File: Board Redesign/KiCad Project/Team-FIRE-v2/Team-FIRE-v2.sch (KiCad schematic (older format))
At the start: 0 parts

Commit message: Added 9523 User Manual
- Added 9523 User manual
- Started work on redesign schematic
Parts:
- added C?: 10uF, Capacitor_SMD:C_0603_1608Metric, symbol Device:C
- added C?: 0.1uF, Capacitor_SMD:C_0603_1608Metric, symbol Device:C
- added C?: 22nF, Capacitor_SMD:C_0603_1608Metric, symbol Device:C
- added C?: 50pF, Capacitor_SMD:C_0603_1608Metric, symbol Device:C
- added C?: 1uF, Capacitor_SMD:C_0603_1608Metric, symbol Device:C
- added C?: 0.1u, Capacitor_SMD:C_0603_1608Metric, symbol Device:C
- added IC?: LT3959EUHE#PBF, Team-FIRE:LT3959EUHEPBF, symbol Team-FIRE:LT3959EUHE#PBF
- added J?: SIM_Card, symbol Connector:SIM_Card
- added R?: 10k, Resistor_SMD:R_0603_1608Metric, symbol Device:R
- added R? (x2): 3.3k, Resistor_SMD:R_0603_1608Metric, symbol Device:R
- added R?: 59k, Resistor_SMD:R_0603_1608Metric, symbol Device:R
- added U?: NCN4555MN, Package_DFN_QFN:QFN-16-1EP_3x3mm_P0.5mm_EP1.75x1.75mm, symbol Logic_LevelTranslator:NCN4555MN
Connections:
- new net: IC?.28 (DRIVE), R?.1
- new net: C?.2, IC?.30 (VC), R?.2
- new net: C?.1, IC?.32 (SS)
- new net: IC?.33 (RT), R?.2
- new net: C?.1, IC?.36 (INTVCC), R?.1
- new net: C?.2, R?.1
- new net +30V: IC?.31 (FBX), R?.1, R?.2
- new net GND: C?.2, C?.2, IC?.13 (GND_1), IC?.14 (GND_2), IC?.15 (GND_3), IC?.16 (GND_4), IC?.17 (GND_5), J?.5 (GND), U?.10 (GND), U?.17 (GND)
- new net GNDA: C?.1, C?.1, C?.2, C?.2, R?.2
- new net GNDS: IC?.1 (NC_1), IC?.12 (GNDK), IC?.2 (NC_2), IC?.23 (NC_6), IC?.24 (SGND_2), IC?.3 (NC_3), IC?.34 (SYNC), IC?.37 (SGND_3), IC?.4 (SGND_1), IC?.6 (NC_4)
- new net IR_5V: C?.1, U?.3 (VDD), U?.5 (VBAT)
- new net IR_SIM_CLK: U?.13 (CLK)
- new net IR_SIM_IO: U?.15 (I/O)
- new net IR_SIM_RESET: U?.14 (RST)
- new net IR_SIM_VCC: U?.2 (MOD_VCC)
- new net SIM_CLOCK: J?.3 (CLK), U?.11 (SIM_CLK)
- new net SIM_IO: J?.7 (I/O), U?.8 (SIM_I/O)
- new net SIM_RESET: J?.2 (RST), U?.9 (SIM_RST)
- new net SIM_VCC: C?.1, J?.1 (VCC), U?.7 (SIM_VCC)
- no-connect marks 0 -> 1
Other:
- note added: "LT3959 Boost"
- note added: "SIM NCN4555 & Card Holder\n"

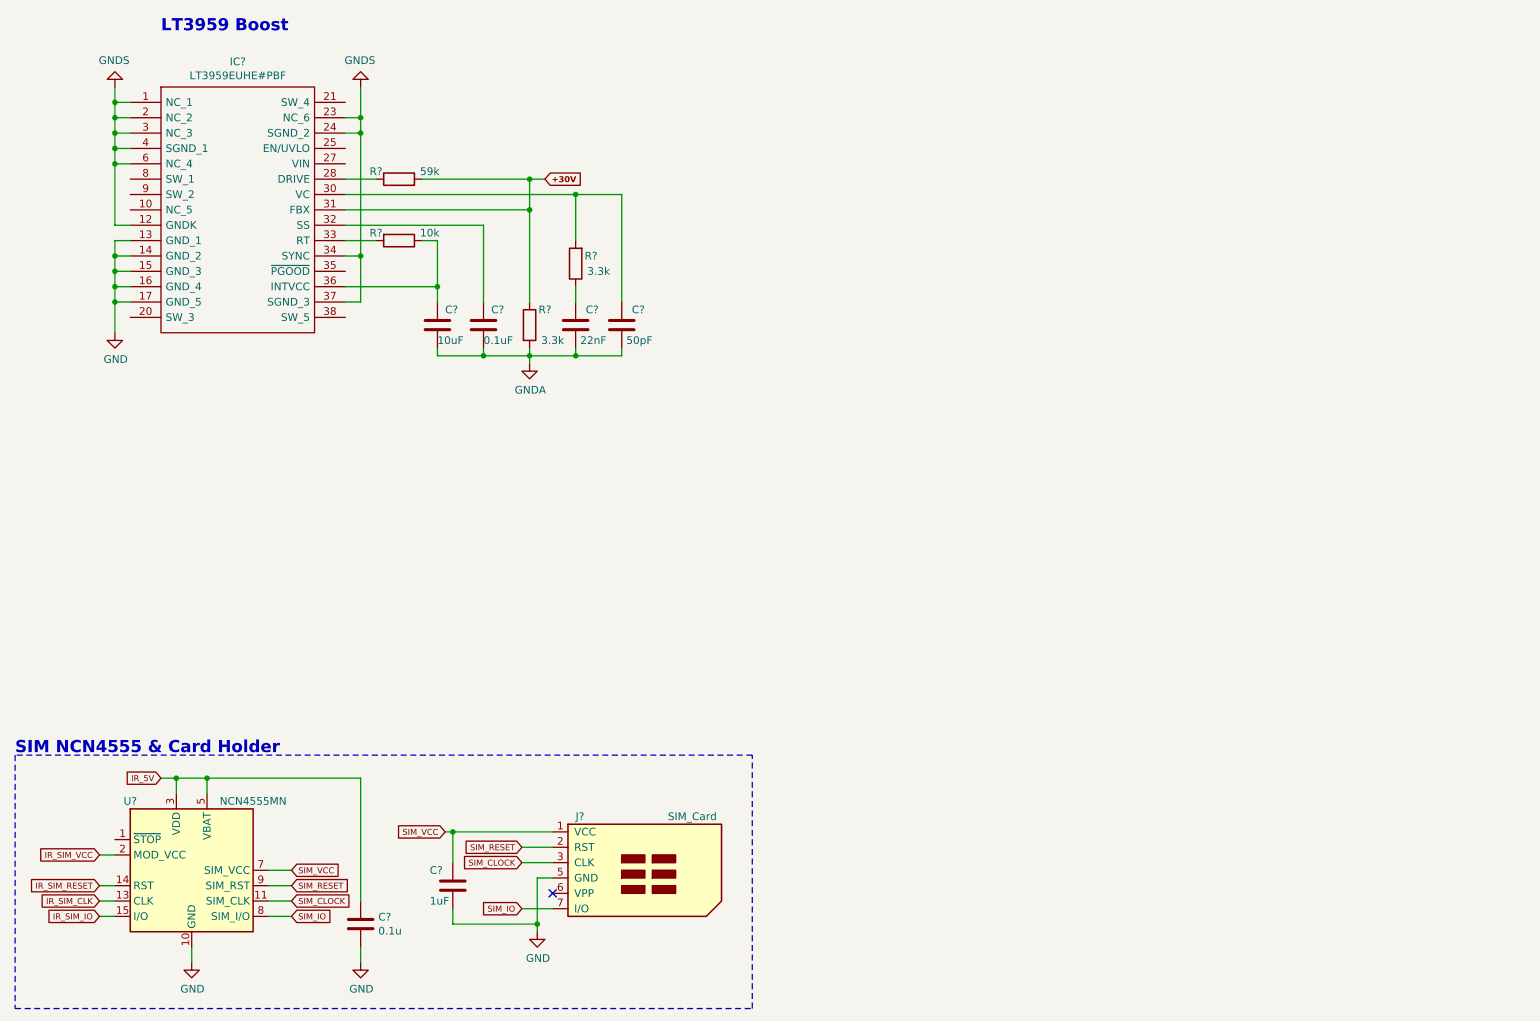
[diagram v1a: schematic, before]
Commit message: Worked more on board!
- Moved more of the schematic over to KiCad
- Created models and footprints / symbols for a few components
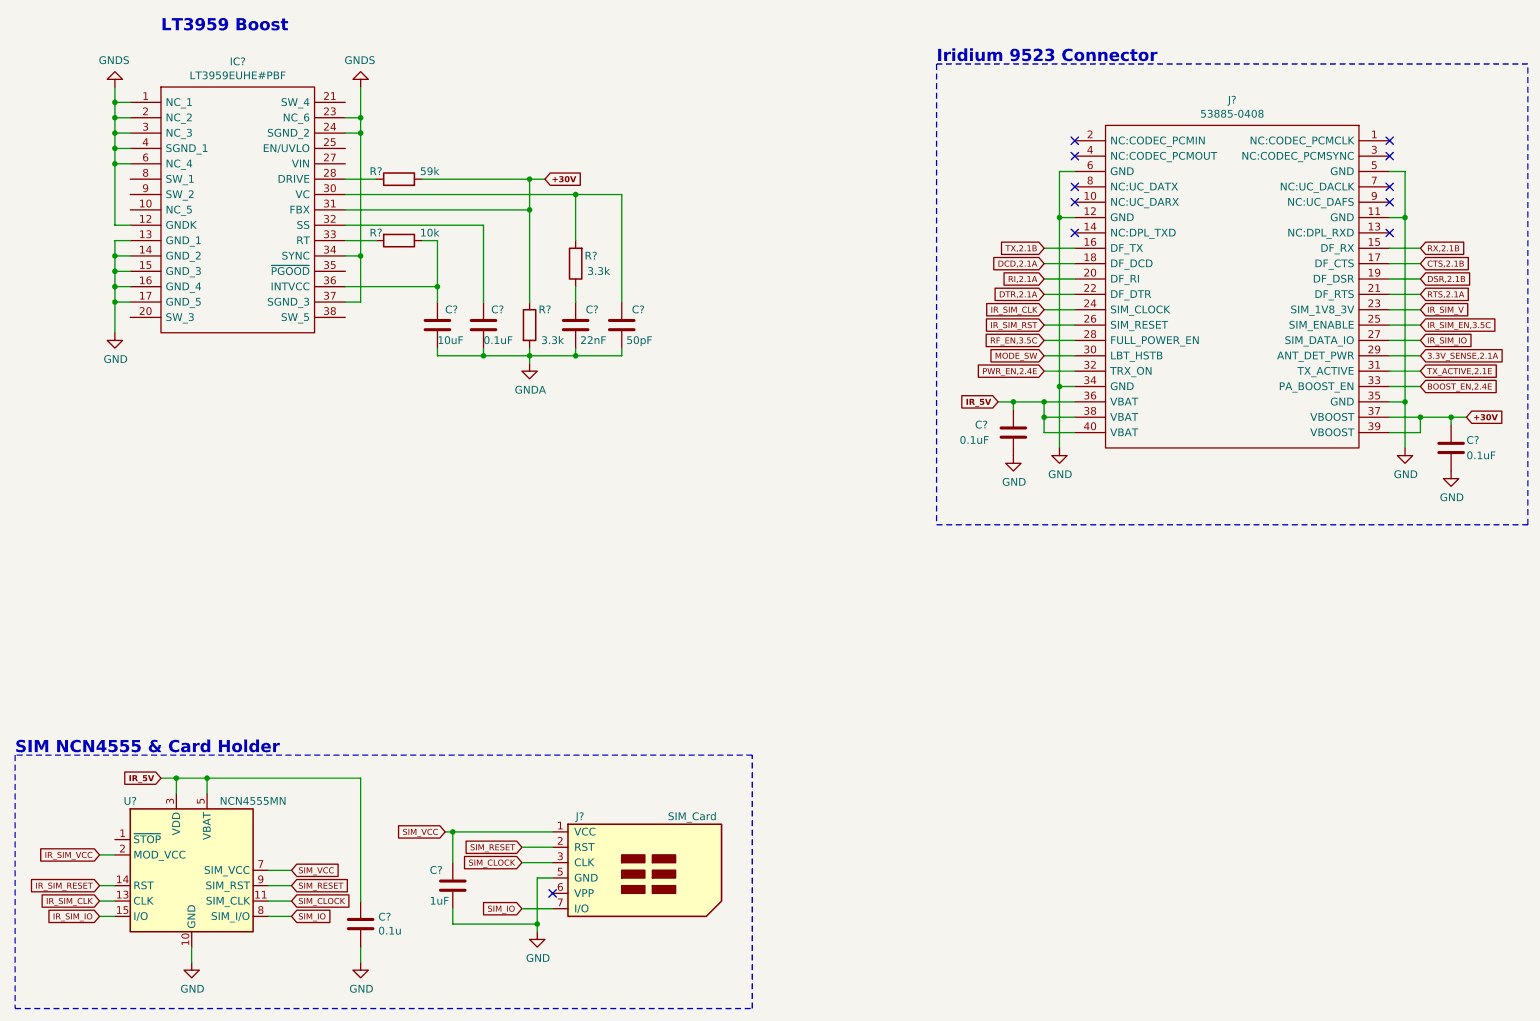
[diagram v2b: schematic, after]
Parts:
- added C? (x2): 0.1uF, Capacitor_SMD:C_0603_1608Metric, symbol Device:C
- added J?: 53885-0408, Team-FIRE:538850408, symbol Team-FIRE:53885-0408
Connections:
- net +30V: now also C?.1, J?.37 (VBOOST), J?.39 (VBOOST)
- net GND: now also C?.2, C?.2, J?.11 (GND), J?.12 (GND), J?.34 (GND), J?.35 (GND), J?.5 (GND), J?.6 (GND)
- net IR_5V: now also C?.1, J?.36 (VBAT), J?.38 (VBAT), J?.40 (VBAT)
- net IR_SIM_CLK: now also J?.24 (SIM_CLOCK)
- net IR_SIM_IO: now also J?.27 (SIM_DATA_IO)
- new net 3.3V_SENSE,2.1A: J?.29 (ANT_DET_PWR)
- new net BOOST_EN,2.4E: J?.33 (PA_BOOST_EN)
- new net CTS,2.1B: J?.17 (DF_CTS)
- new net DCD,2.1A: J?.18 (DF_DCD)
- new net DSR,2.1B: J?.19 (DF_DSR)
- new net DTR,2.1A: J?.22 (DF_DTR)
- new net IR_SIM_EN,3.5C: J?.25 (SIM_ENABLE)
- new net IR_SIM_RST: J?.26 (SIM_RESET)
- new net IR_SIM_V: J?.23 (SIM_1V8_3V)
- new net MODE_SW: J?.30 (LBT_HSTB)
- new net PWR_EN,2.4E: J?.32 (TRX_ON)
- new net RF_EN,3.5C: J?.28 (FULL_POWER_EN)
- new net RI,2.1A: J?.20 (DF_RI)
- new net RTS,2.1A: J?.21 (DF_RTS)
- new net RX,2.1B: J?.15 (DF_RX)
- new net TX,2.1B: J?.16 (DF_TX)
- new net TX_ACTIVE,2.1E: J?.31 (TX_ACTIVE)
- no-connect marks 1 -> 11
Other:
- note added: "Iridium 9523 Connector\n"

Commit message: Hecho más progreso
- Added I2C bus converter
- Added all voltage translators
- Created hierarchical schematics
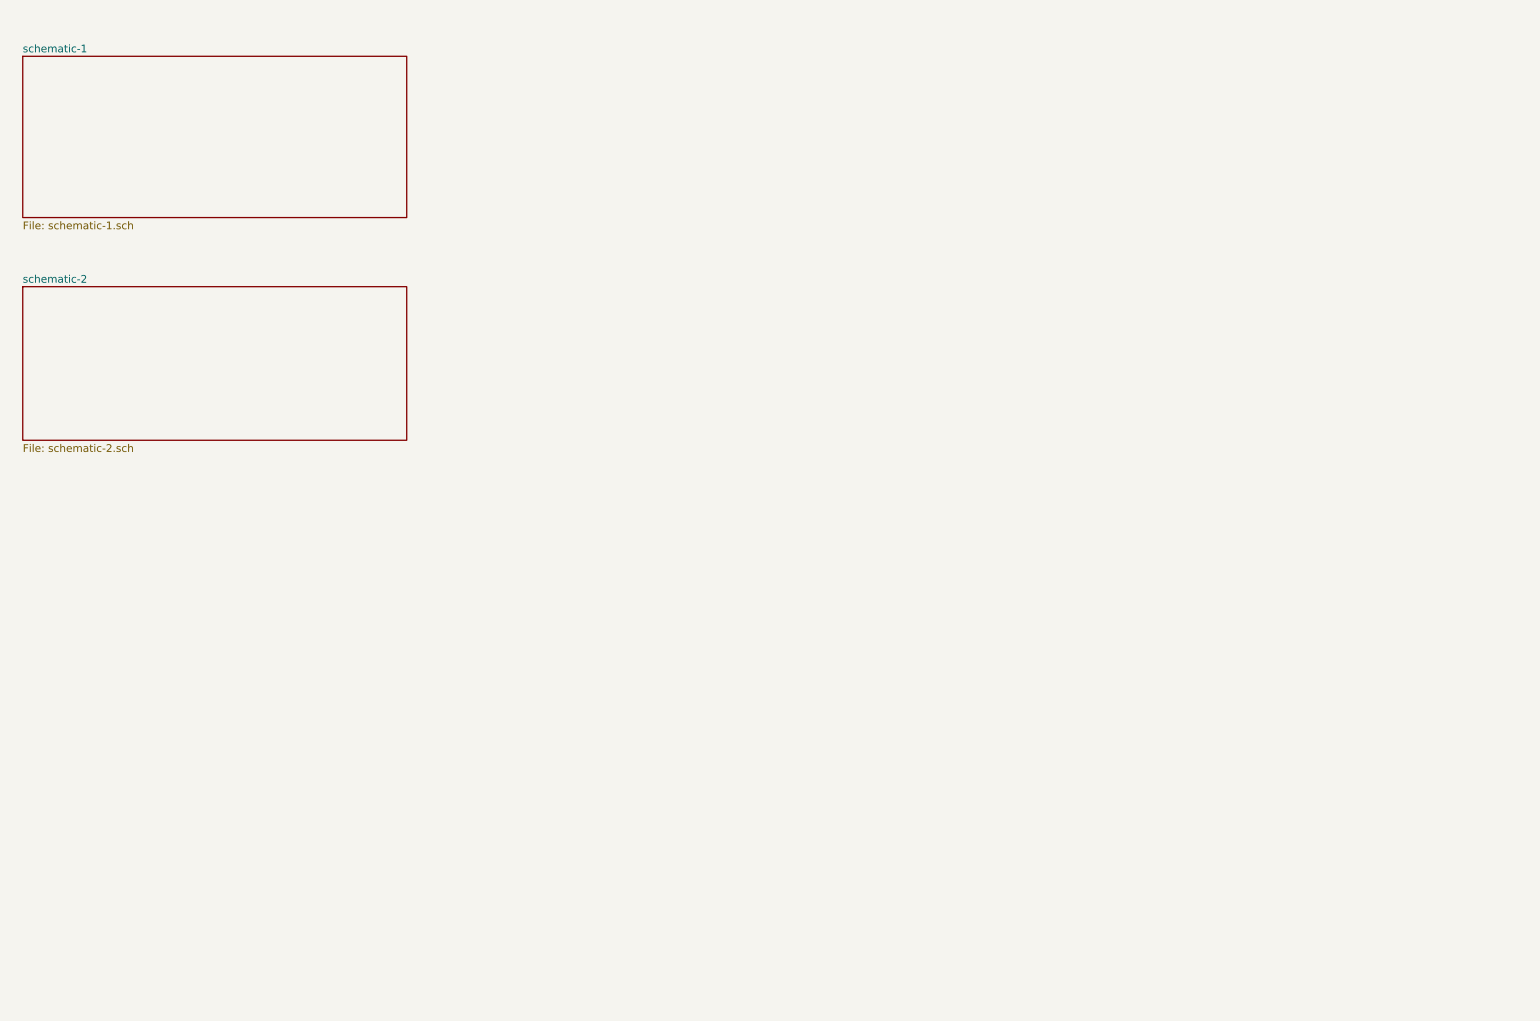
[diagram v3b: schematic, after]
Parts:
- removed C?: 10uF, Capacitor_SMD:C_0603_1608Metric, symbol Device:C
- removed C? (x3): 0.1uF, Capacitor_SMD:C_0603_1608Metric, symbol Device:C
- removed C?: 22nF, Capacitor_SMD:C_0603_1608Metric, symbol Device:C
- removed C?: 50pF, Capacitor_SMD:C_0603_1608Metric, symbol Device:C
- removed C?: 1uF, Capacitor_SMD:C_0603_1608Metric, symbol Device:C
- removed C?: 0.1u, Capacitor_SMD:C_0603_1608Metric, symbol Device:C
- removed IC?: LT3959EUHE#PBF, Team-FIRE:LT3959EUHEPBF, symbol Team-FIRE:LT3959EUHE#PBF
- removed J?: SIM_Card, symbol Connector:SIM_Card
- removed J?: 53885-0408, Team-FIRE:538850408, symbol Team-FIRE:53885-0408
- removed R?: 10k, Resistor_SMD:R_0603_1608Metric, symbol Device:R
- removed R? (x2): 3.3k, Resistor_SMD:R_0603_1608Metric, symbol Device:R
- removed R?: 59k, Resistor_SMD:R_0603_1608Metric, symbol Device:R
- removed U?: NCN4555MN, Package_DFN_QFN:QFN-16-1EP_3x3mm_P0.5mm_EP1.75x1.75mm, symbol Logic_LevelTranslator:NCN4555MN
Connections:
- no-connect marks 11 -> 0
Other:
- note removed: "Iridium 9523 Connector\n"
- note removed: "LT3959 Boost"
- note removed: "SIM NCN4555 & Card Holder\n"

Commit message: Added Shelby's work
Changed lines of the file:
@@
 $Descr A4 11693 8268
 encoding utf-8
-Sheet 1 3
+Sheet 1 4
 Title "Team FIRE Board Redesign"
 Date "2020-02-20"
@@
 F1 "schematic-2.sch" 50
 $EndSheet
+$Sheet
+S 1000 3950 2500 1050
+U 5E585515
+F0 "schematic-3" 50
+F1 "schematic-3.sch" 50
+$EndSheet
 $EndSCHEMATC

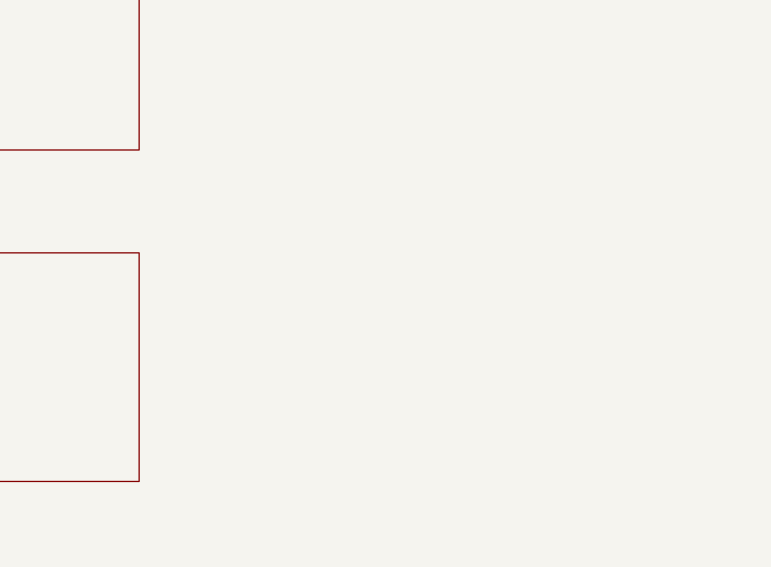
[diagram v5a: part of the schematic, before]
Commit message: Added SAMD51
- Created schematic symbol, footprint, and 3D model for the SAMD51
- Added SAMD51 to the schematic (only partially implemented)
- Added decoupling capacitors to the 3.3V bus (as recommended by the SAMD51 design manual)
- Started checklist for SAMD51 implementation on the top-level schematic sheet; there's no convenient breakout board to emulate
- Implemented power connections for SAMD51
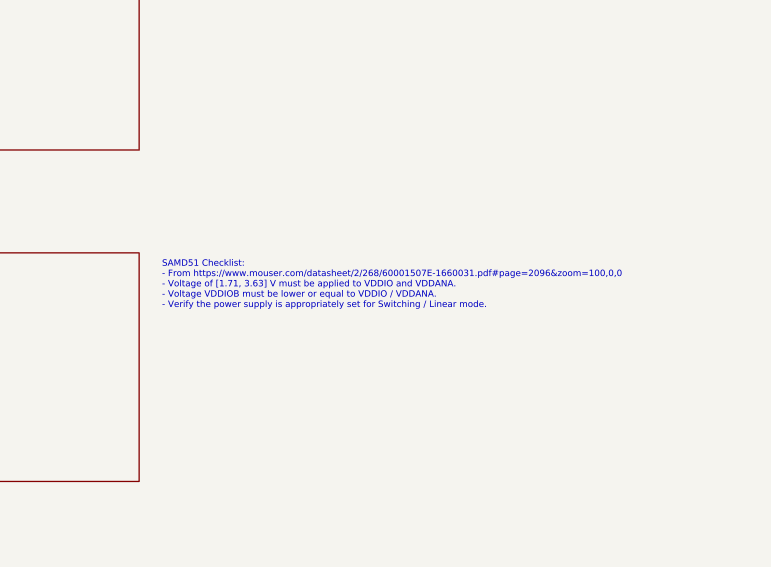
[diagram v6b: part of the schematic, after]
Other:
- note added: "SAMD51 Checklist:\n- From https://www.mouser.com/datasheet/2/268/60001507E-1660031.pdf#page=2096&zoom=100,0,0\n- Voltage of [1.71, 3.63] V must be applied to VDDIO and VDDANA.\n- Voltage VDDIOB must be lower or equal to VDDIO / VDDANA.\n- Verify the power supply is appropriately set for Switching / Linear mode."
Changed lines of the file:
@@
 F1 "schematic-3.sch" 50
 $EndSheet
+Text Notes 3600 2750 0    28   ~ 0
+SAMD51 Checklist:\n- From https://www.mouser.com/datasheet/2/268/60001507E-1660031.pdf#page=2096&zoom=100,0,0\n- Voltage of [1.71, 3.63] V must be applied to VDDIO and VDDANA.\n- Voltage VDDIOB must be lower or equal to VDDIO / VDDANA.\n- Verify the power supply is appropriately set for Switching / Linear mode.
 $EndSCHEMATC
